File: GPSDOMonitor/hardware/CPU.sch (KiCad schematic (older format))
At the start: 4 parts, among them U1 PIC18LF2550-ISO, X1 ABM8W-20.0000MHZ-4-K1Z-T3

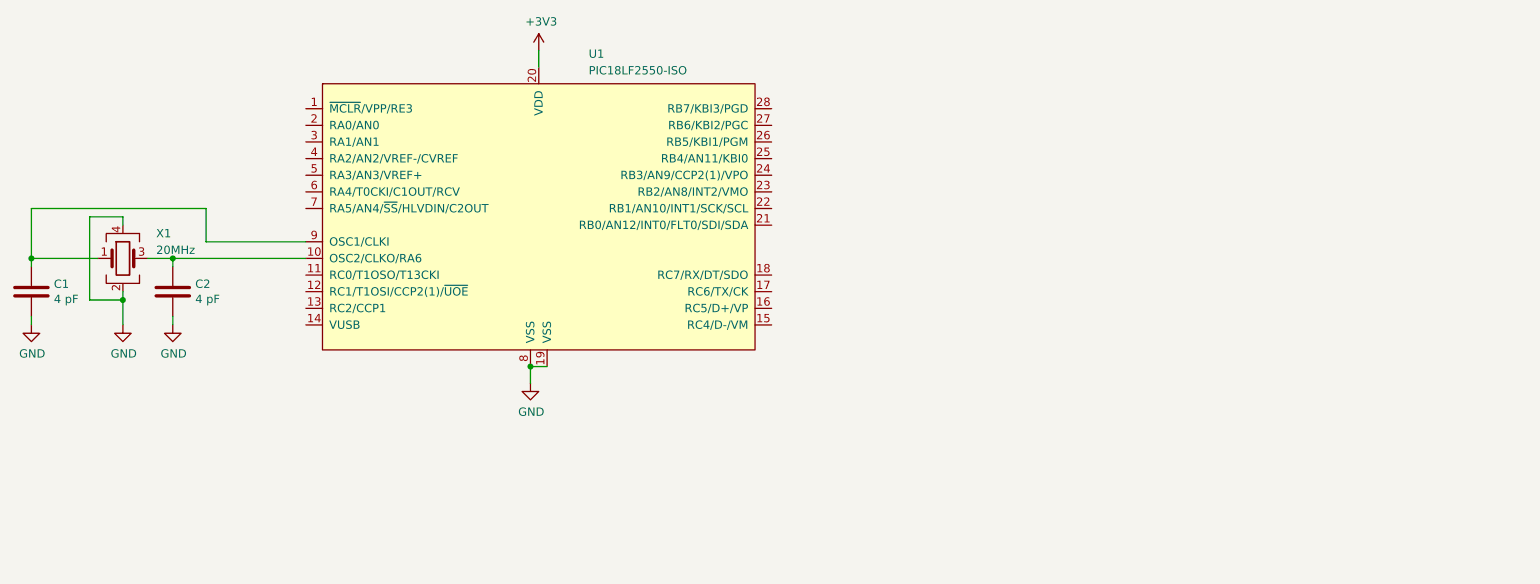
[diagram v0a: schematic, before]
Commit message: Add connector for the GPSDO
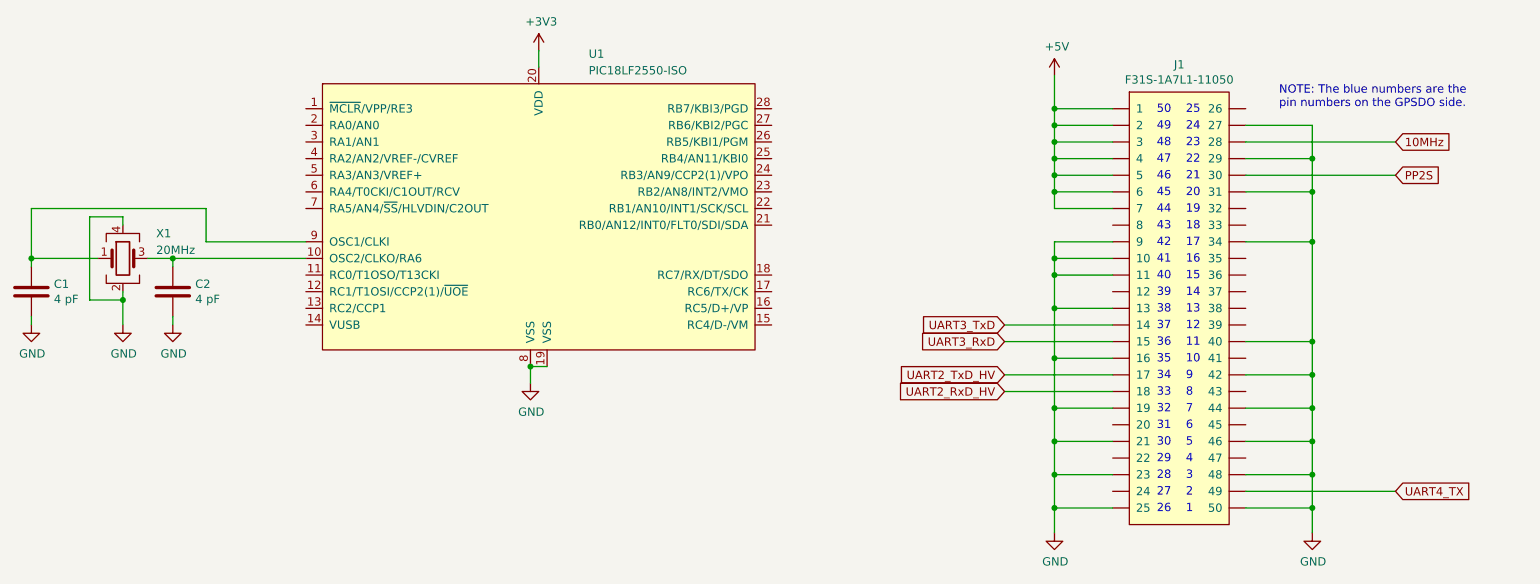
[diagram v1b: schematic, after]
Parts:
- added J1: F31S-1A7L1-11050, Connector_Data:F31S-1A7L1-11050, symbol Connector_Data:F31S-1A7L1-11050
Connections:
- net GND: now also J1.10, J1.11, J1.13, J1.16, J1.19, J1.21, J1.23, J1.25, J1.27, J1.29, J1.31, J1.34, J1.40, J1.42, J1.44, J1.46, J1.48, J1.50, J1.9
- new net +5V: J1.1, J1.2, J1.3, J1.4, J1.5, J1.6, J1.7
- new net 10MHz: J1.28
- new net PP2S: J1.30
- new net UART2_RxD_HV: J1.18
- new net UART2_TxD_HV: J1.17
- new net UART3_RxD: J1.15
- new net UART3_TxD: J1.14
- new net UART4_TX: J1.49
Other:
- note added: "1"
- note added: "10"
- note added: "11"
- note added: "12"
- note added: "13"
- note added: "14"
- note added: "15"
- note added: "16"
- note added: "17"
- note added: "18"
- note added: "19"
- note added: "2"
- note added: "20"
- note added: "21"
- note added: "22"
- note added: "23"
- note added: "24"
- note added: "25"
- note added: "26"
- note added: "27"
- note added: "28"
- note added: "29"
- note added: "3"
- note added: "30"
- note added: "31"
- note added: "32"
- note added: "33"
- note added: "34"
- note added: "35"
- note added: "36"
- note added: "37"
- note added: "38"
- note added: "39"
- note added: "4"
- note added: "40"
- note added: "41"
- note added: "42"
- note added: "43"
- note added: "44"
- note added: "45"
- note added: "46"
- note added: "47"
- note added: "48"
- note added: "49"
- note added: "5"
- note added: "50"
- note added: "6"
- note added: "7"
- note added: "8"
- note added: "9"
- note added: "NOTE: The blue numbers are the\npin numbers on the GPSDO side."
